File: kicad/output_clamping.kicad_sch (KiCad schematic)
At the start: 43 parts, among them J4 Output, SW3 SW_SPDT, SW4 SW_SPDT, U12 OPA189, U13 BUF634A, U15 LM4040DBZ-5, U16 LM4040DBZ-5, U24 LM4040DBZ-5, U25 LM4040DBZ-5, U26 OPA189, U27 OPA189, U28 LM4040DBZ-5, U29 LM4040DBZ-5, U30 LM4040DBZ-5, U31 LM4040DBZ-5, U32 LM4040DBZ-5, U33 LM4040DBZ-5, U34 TMUX6123, U6 OPA189

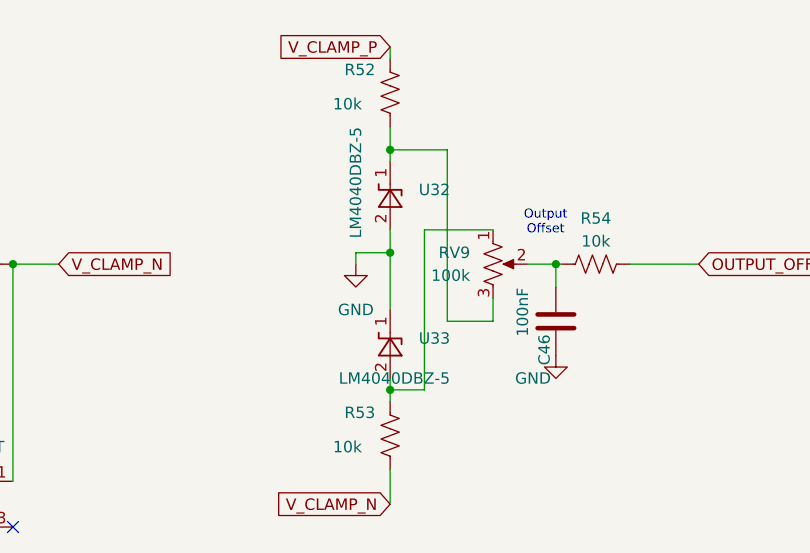
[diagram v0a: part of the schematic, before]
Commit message: Remove ground in between P and N clamps, as they can be the same sign
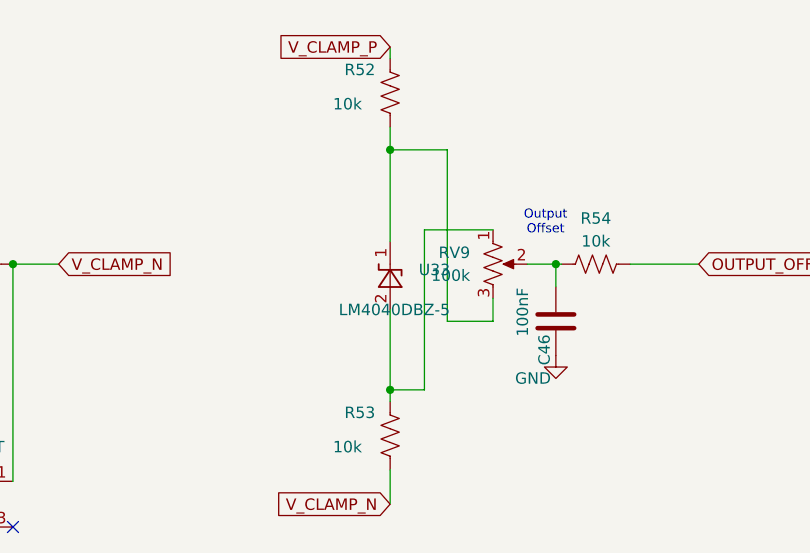
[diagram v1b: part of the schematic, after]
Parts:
- removed U32: LM4040DBZ-5, Package_TO_SOT_SMD:SOT-23, symbol Reference_Voltage:LM4040DBZ-5
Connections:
- net GND: no longer U33.1 (K)
- net at R52.1, RV9.3: now also U33.1 (K)
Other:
- moved on the sheet: U33
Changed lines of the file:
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@@
 	)
 	(junction
-		(at 190.5 55.88)
-		(diameter 0)
-		(color 0 0 0 0)
-	)
-	(junction
 		(at 208.915 57.15)
 		(diameter 0)
@@
 	(wire
 		(pts
-			(xy 190.5 55.88) (xy 190.5 62.23)
-		)
-		(stroke
-			(width 0)
-			(type default)
-		)
-	)
-	(wire
-		(pts
-			(xy 190.5 44.45) (xy 190.5 45.72)
-		)
-		(stroke
-			(width 0)
-			(type default)
-		)
-	)
-	(wire
-		(pts
 			(xy 156.21 146.05) (xy 156.21 142.24)
 		)
@@
 	(wire
 		(pts
-			(xy 190.5 69.85) (xy 190.5 71.12)
+			(xy 190.5 62.23) (xy 190.5 71.12)
 		)
 		(stroke
@@
 	(wire
 		(pts
-			(xy 190.5 53.34) (xy 190.5 55.88)
-		)
-		(stroke
-			(width 0)
-			(type default)
-		)
-	)
-	(wire
-		(pts
 			(xy 248.92 85.09) (xy 248.92 88.9)
 		)
@@
 	(wire
 		(pts
-			(xy 186.69 55.88) (xy 190.5 55.88)
-		)
-		(stroke
-			(width 0)
-			(type default)
-		)
-	)
-	(wire
-		(pts
 			(xy 129.54 143.51) (xy 133.35 143.51)
 		)
@@
 	(wire
 		(pts
-			(xy 186.69 57.15) (xy 186.69 55.88)
-		)
-		(stroke
-			(width 0)
-			(type default)
-		)
-	)
-	(wire
-		(pts
 			(xy 190.5 71.12) (xy 190.5 72.39)
 		)
@@
 	(wire
 		(pts
+			(xy 190.5 44.45) (xy 190.5 54.61)
+		)
+		(stroke
+			(width 0)
+			(type default)
+		)
+	)
+	(wire
+		(pts
 			(xy 213.36 97.79) (xy 213.36 99.06)
 		)
@@
 	(symbol
 		(lib_id "Reference_Voltage:LM4040DBZ-5")
-		(at 190.5 66.04 90)
+		(at 190.5 58.42 90)
 		(unit 1)
 		(exclude_from_sim no)
@@
 		(dnp no)
 		(property "Reference" "U33"
-			(at 193.675 65.405 90)
+			(at 193.675 57.785 90)
 			(effects
 				(font
@@
 		)
 		(property "Value" "LM4040DBZ-5"
-			(at 184.785 69.85 90)
+			(at 184.785 62.23 90)
 			(effects
 				(font
@@
 		)
 		(property "Footprint" "Package_TO_SOT_SMD:SOT-23"
-			(at 195.58 66.04 0)
+			(at 195.58 58.42 0)
 			(effects
 				(font
@@
 		)
 		(property "Datasheet" "http://www.ti.com/lit/ds/symlink/lm4040-n.pdf"
-			(at 190.5 66.04 0)
+			(at 190.5 58.42 0)
 			(effects
 				(font
@@
 		)
 		(property "Description" ""
-			(at 190.5 66.04 0)
+			(at 190.5 58.42 0)
 			(effects
 				(font
@@
 		)
 		(property "PARTNO" "LM4040B50FTA"
-			(at 190.5 66.04 90)
+			(at 190.5 58.42 90)
 			(effects
 				(font
@@
 		)
 		(property "DIGIKEY" "LM4040B50FTADICT-ND"
-			(at 190.5 66.04 90)
+			(at 190.5 58.42 90)
 			(effects
 				(font
@@
 		)
 		(property "MPN" ""
-			(at 190.5 66.04 90)
+			(at 190.5 58.42 90)
 			(effects
 				(font
@@
 	)
 	(symbol
-		(lib_id "power:GND")
-		(at 186.69 57.15 0)
-		(unit 1)
-		(exclude_from_sim no)
-		(in_bom yes)
-		(on_board yes)
-		(dnp no)
-		(fields_autoplaced yes)
-		(property "Reference" "#PWR099"
-			(at 186.69 63.5 0)
-			(effects
-				(font
-					(size 1.27 1.27)
-				)
-				(hide yes)
-			)
-		)
-		(property "Value" "GND"
-			(at 186.69 62.23 0)
-			(effects
-				(font
-					(size 1.27 1.27)
-				)
-			)
-		)
-		(property "Footprint" ""
-			(at 186.69 57.15 0)
-			(effects
-				(font
-					(size 1.27 1.27)
-				)
-				(hide yes)
-			)
-		)
-		(property "Datasheet" ""
-			(at 186.69 57.15 0)
-			(effects
-				(font
-					(size 1.27 1.27)
-				)
-				(hide yes)
-			)
-		)
-		(property "Description" ""
-			(at 186.69 57.15 0)
-			(effects
-				(font
-					(size 1.27 1.27)
-				)
-				(hide yes)
-			)
-		)
-		(pin "1"
-		)
-		(instances
-			(project "intensity_pi"
-				(path "/3a3d7bcb-6fa5-41ef-9ea1-6d4ab7c492fd/e5e2bc93-86a3-4c55-a500-b723f214f000"
-					(reference "#PWR099")
-					(unit 1)
-				)
-			)
-		)
-	)
-	(symbol
 		(lib_id "power:-15V")
 		(at 81.28 154.94 180)
@@
 					(unit 1)
 				)
-			)
-		)
-	)
-	(symbol
-		(lib_id "Reference_Voltage:LM4040DBZ-5")
-		(at 190.5 49.53 90)
-		(unit 1)
-		(exclude_from_sim no)
-		(in_bom yes)
-		(on_board yes)
-		(dnp no)
-		(property "Reference" "U32"
-			(at 193.675 48.895 90)
-			(effects
-				(font
-					(size 1.27 1.27)
-				)
-				(justify right)
-			)
-		)
-		(property "Value" "LM4040DBZ-5"
-			(at 186.69 41.91 0)
-			(effects
-				(font
-					(size 1.27 1.27)
-				)
-				(justify right)
-			)
-		)
-		(property "Footprint" "Package_TO_SOT_SMD:SOT-23"
-			(at 195.58 49.53 0)
-			(effects
-				(font
-					(size 1.27 1.27)
-					(italic yes)
-				)
-				(hide yes)
-			)
-		)
-		(property "Datasheet" "http://www.ti.com/lit/ds/symlink/lm4040-n.pdf"
-			(at 190.5 49.53 0)
-			(effects
-				(font
-					(size 1.27 1.27)
-					(italic yes)
-				)
-				(hide yes)
-			)
-		)
-		(property "Description" ""
-			(at 190.5 49.53 0)
-			(effects
-				(font
-					(size 1.27 1.27)
-				)
-				(hide yes)
-			)
-		)
-		(property "PARTNO" "LM4040B50FTA"
-			(at 190.5 49.53 90)
-			(effects
-				(font
-					(size 1.27 1.27)
-				)
-				(hide yes)
-			)
-		)
-		(property "DIGIKEY" "LM4040B50FTADICT-ND"
-			(at 190.5 49.53 90)
-			(effects
-				(font
-					(size 1.27 1.27)
-				)
-				(hide yes)
-			)
-		)
-		(property "MPN" ""
-			(at 190.5 49.53 90)
-			(effects
-				(font
-					(size 1.27 1.27)
-				)
-				(hide yes)
-			)
-		)
-		(pin "1"
-		)
-		(pin "2"
-		)
-		(instances
-			(project "intensity_pi"
-				(path "/3a3d7bcb-6fa5-41ef-9ea1-6d4ab7c492fd/e5e2bc93-86a3-4c55-a500-b723f214f000"
-					(reference "U32")
-					(unit 1)
-				)

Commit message: Updated schematic and design
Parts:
- removed R52, R53, R54: 10k, Resistor_SMD:R_0805_2012Metric, symbol Device:R_US
- removed U15, U16, U24, U25, U28, U29, U30, U31, U33: LM4040DBZ-5, Package_TO_SOT_SMD:SOT-23, symbol Reference_Voltage:LM4040DBZ-5
- removed U34: TMUX6123, Package_SO:VSSOP-10_3x3mm_P0.5mm, symbol library_intensity_pi:TMUX6123_split
- removed U6: OPA189, Package_SO:SOIC-8_3.9x4.9mm_P1.27mm, symbol Amplifier_Operational:OPA330xxD
- added D2, D4, D5, D6: D, Package_TO_SOT_SMD:TSOT-23, symbol Device:D
- added U32, U9: OPA189, Package_SO:SOIC-8_3.9x4.9mm_P1.27mm, symbol Amplifier_Operational:OPA330xxD
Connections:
- net +15V: now also U32.7 (V+), U9.7 (V+)
- net -15V: now also U32.4 (V-), U9.4 (V-)
- net OUTPUT_OFFSET: now also C46.2, RV9.2
- net V_CLAMP_N: now also U32.3 (+)
- net V_CLAMP_P: now also U9.3 (+)
- net V_PI_OUT: now also R47.1
- net at C12.2, R22.1, R47.2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: now also D4.1 (K), D5.3 (A)
- net at C12.1, R22.2, U13.6 (OUT): now also R23.1, R48.2, R49.2
- net at RV9.3: now also U9.2 (-), U9.6
- net at RV9.1: now also U32.2 (-), U32.6
- net at C27.2, U26.6: now also D2.1 (K), D4.3 (A)
- net at C27.1, R48.1, U26.2 (-): now also D2.3 (A)
- net at C22.2, U27.6: now also D5.1 (K), D6.3 (A)
- net at C22.1, R49.1, U27.2 (-): now also D6.1 (K)
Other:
- moved on the sheet: C12, C22, C27, C34, C35, J4, R12, R14, R22, R23, R35, R42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

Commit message: First pass at updated schematic and loose PCB grouping, TODO: Fix PI Gain values
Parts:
- removed J4: Output, Connector_Coaxial:BNC_Amphenol_B6252HB-NPP3G-50_Horizontal, symbol Connector:Conn_Coaxial
- removed R42, R45: 10k, Resistor_SMD:R_0805_2012Metric, symbol Device:R_US
- added J6: Conn_Coaxial_x2_Isolated, Connector_Coaxial:BNC_Amphenol_031-6575_Horizontal, symbol Connector:Conn_Coaxial_x2_Isolated
- added R56, R58: 1k, Resistor_SMD:R_0805_2012Metric, symbol Device:R_US
- added SW5, SW6: SW_SPDT, Custom_Footprints:TDD DIP Switch, symbol Switch:SW_SPDT
- R52: renamed from R12; value 10k -> 1k; DIGIKEY 2019-RN73H2ATTD1002B25CT-ND -> (none); PARTNO RN73H2ATTD1002B25 -> (none)
- R53: renamed from R14; value 10k -> 1k; DIGIKEY 2019-RN73H2ATTD1002B25CT-ND -> (none); PARTNO RN73H2ATTD1002B25 -> (none)
- RV5: renamed from RV6; Tag (none) -> V+ Limiit
- RV6: renamed from RV7; Tag (none) -> V- Limit
- RV7: renamed from RV9; Tag (none) -> Output Offset
- U22: renamed from U13; footprint lib:TI_SO-PowerPAD-8_ThermalVias -> Custom_Footprints:BUF634AIDDAR
- renumbered C34 to C56, C12 to C57, C35 to C58, C27 to C59, C46 to C60, C22 to C61, D4 to D3, D6 to D4, R47 to R54, R50 to R55, R22 to R57, R51 to R59, R35 to R60, R48 to R61, R49 to R62, R23 to R63, U12 to U21, U26 to U23, U9 to U24, U32 to U25, U27 to U26
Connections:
- net +15V: now also SW5.3 (C)
- net -15V: now also SW3.3 (C), R56.1; no longer R53.1
- net GND: now also SW3.1 (A), SW4.1 (A), J6.2 (Ext1), SW5.1 (A), SW6.1 (A); no longer SW3.2 (B), SW4.2 (B)
- net V_CLAMP_N: now also SW6.2 (B); no longer SW3.1 (A)
- net V_CLAMP_P: now also SW4.2 (B); no longer SW4.1 (A)
- net at C61.2, D5.1 (K), U26.6: now also D4.2 (A); no longer D4.3 (A)
- net at C57.2, D3.1 (K), R54.2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: now also D5.2 (A); no longer D5.3 (A)
- net at R63.2: now also J6.1 (In1)
- net at C59.1, R61.1, U23.2 (-): now also D2.2 (A); no longer D2.3 (A)
- net at RV6.1: now also R56.2
- net at RV6.3: now also R58.1
- net at C59.2, D2.1 (K), U23.6: now also D3.2 (A); no longer D3.3 (A)
- new net: R58.2, SW5.2 (B)
- new net: R53.1, SW3.2 (B)
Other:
- note added: "Limit V+ > 0"
- note added: "Limit V- < 0"
- note added: "Pots: CW moved 2 closer to 3"
- note added: "Set V+ = 0"
- moved on the sheet: C56, C57, C58, C60, R52, R53, R54, R55, R59, RV5, RV6, SW4

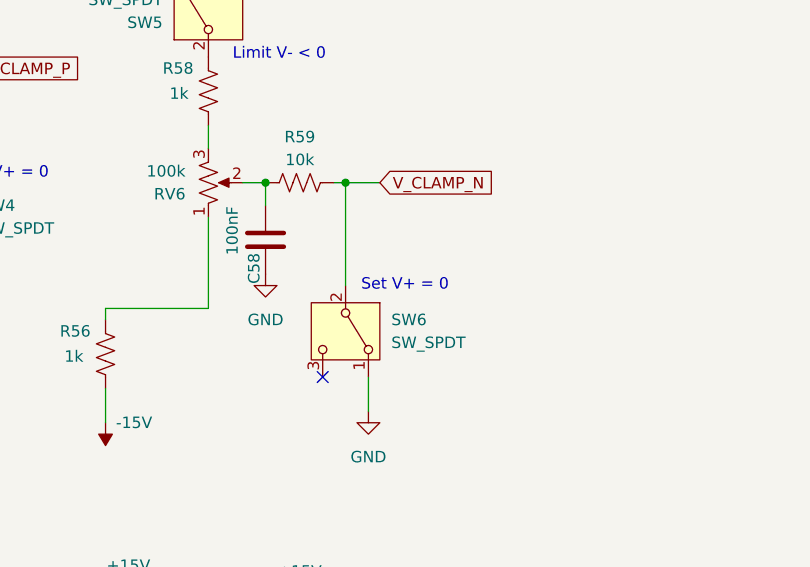
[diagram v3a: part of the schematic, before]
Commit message: Added Test Board to test various gain control as well as clamping mechanism
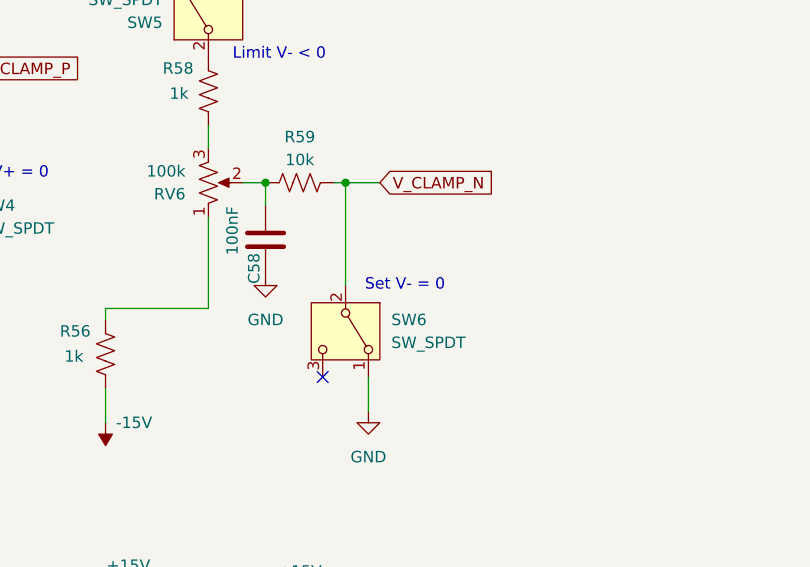
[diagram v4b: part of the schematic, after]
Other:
- note added: "Set V- = 0"
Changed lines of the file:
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@@
 		)
 	)
-	(text "Set V+ = 0"
+	(text "Set V- = 0"
 		(exclude_from_sim no)
 		(at 98.044 64.77 0)
